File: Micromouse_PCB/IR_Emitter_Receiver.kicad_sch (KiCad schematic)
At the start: 36 parts, among them Q1 Q_NMOS_GSD, Q10 AA4040P3C-P22, Q12 Q_NMOS_GSD, Q13 AA4040P3C-P22, Q2 AA4040P3C-P22, Q3 Q_NMOS_GSD, Q4 AA4040P3C-P22, Q5 Q_NMOS_GSD, Q6 AA4040P3C-P22, Q7 Q_NMOS_GSD, Q8 AA4040P3C-P22, Q9 Q_NMOS_GSD

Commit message: Schematic almost done, just need to do STM32 pinout
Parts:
- R10, R13, R16, R22, R3, R6: value 1.8k -> 3.3k
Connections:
- net GND: now also R10.2, R13.2, R16.2, R22.2, R3.2, R6.2; no longer R10.1, R13.1, R16.1, R22.1, R3.1, R6.1
- net RECEIV1: now also R16.1; no longer R22.2
- net RECEIV2: now also R3.1; no longer R3.2
- net RECEIV3: now also R6.1; no longer R6.2
- net RECEIV4: now also R10.1; no longer R10.2
- net RECEIV5: now also R13.1; no longer R13.2
- net RECEIV6: now also R22.1; no longer R16.2
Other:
- moved on the sheet: R16

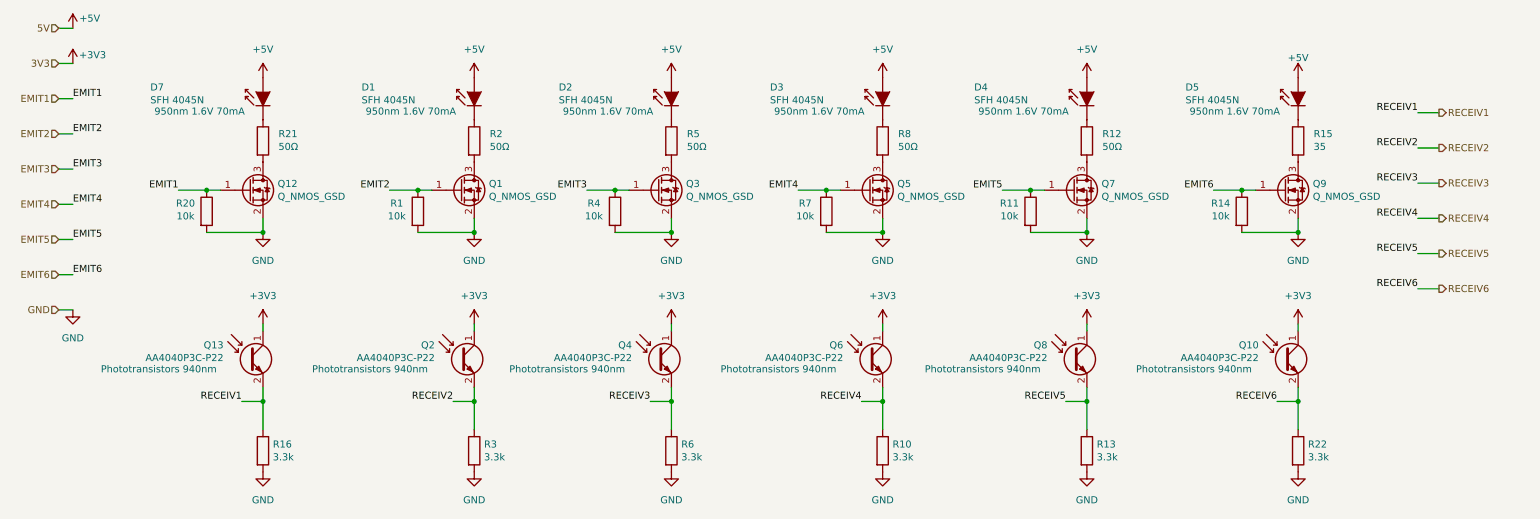
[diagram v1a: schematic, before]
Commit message: Placement 75% done on PCB
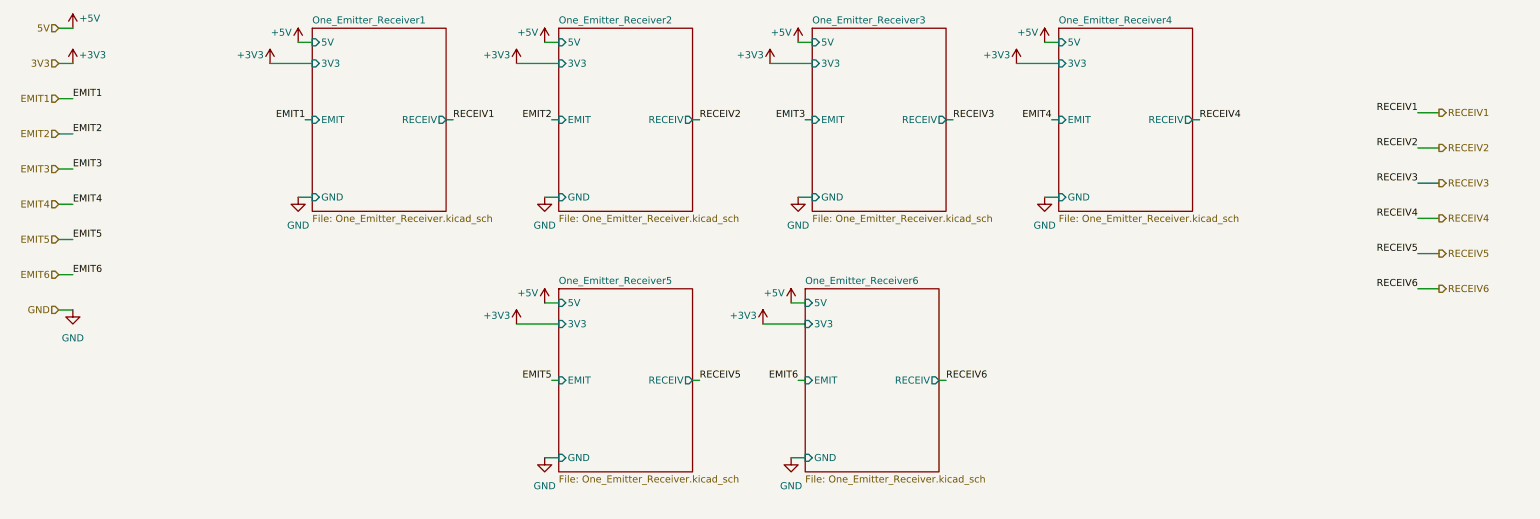
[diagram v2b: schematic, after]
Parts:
- removed D1, D2, D3, D4, D5, D7: SFH 4045N, UCIRP-KiCAD-Lib:IR_Emitter SFH_4045N, symbol bloo-rescue:IRL81A-LED-mouse_v2-rescue
- removed Q1, Q12, Q3, Q5, Q7, Q9: Q_NMOS_GSD, Package_TO_SOT_SMD:SOT-23, symbol Device:Q_NMOS_GSD
- removed Q10, Q13, Q2, Q4, Q6, Q8: AA4040P3C-P22, UCIRP-KiCAD-Lib:Phototransistor AA4040P3C, symbol bloo-rescue:Q_Photo_NPN-Device-mouse_v2-rescue
- removed R1, R11, R14, R20, R4, R7: 10k, Resistor_SMD:R_1206_3216Metric_Pad1.30x1.75mm_HandSolder, symbol bloo-rescue:R-Device-mouse_v2-rescue
- removed R10, R13, R16, R22, R3, R6: 3.3k, Resistor_SMD:R_1206_3216Metric_Pad1.30x1.75mm_HandSolder, symbol bloo-rescue:R-Device-mouse_v2-rescue
- removed R12, R2, R21, R5, R8: 50Ω, Resistor_SMD:R_0603_1608Metric, symbol bloo-rescue:R-Device-mouse_v2-rescue
- removed R15: 35, Resistor_SMD:R_1206_3216Metric_Pad1.30x1.75mm_HandSolder, symbol bloo-rescue:R-Device-mouse_v2-rescue
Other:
- added sheet One_Emitter_Receiver1 (One_Emitter_Receiver.kicad_sch)
- added sheet One_Emitter_Receiver2 (One_Emitter_Receiver.kicad_sch)
- added sheet One_Emitter_Receiver3 (One_Emitter_Receiver.kicad_sch)
- added sheet One_Emitter_Receiver4 (One_Emitter_Receiver.kicad_sch)
- added sheet One_Emitter_Receiver5 (One_Emitter_Receiver.kicad_sch)
- added sheet One_Emitter_Receiver6 (One_Emitter_Receiver.kicad_sch)
